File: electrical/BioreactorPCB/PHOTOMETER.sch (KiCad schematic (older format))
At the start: 9 parts, among them IC2 VEML7700-TR, J11 Conn_01x06_Male, U4 TCA39306DCUR

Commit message: Converted all nonpolarized resistors and capacitors to SMD. USB now has differential pairs that conform to design guidelines. Lots of traces, to what end? idk.
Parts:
- R8: footprint Resistor_THT:R_Axial_DIN0207_L6.3mm_D2.5mm_P10.16mm_Horizontal -> Resistor_SMD:R_0805_2012Metric_Pad1.20x1.40mm_HandSolder
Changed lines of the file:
@@
 F 0 "R8" V 7693 2425 50  0000 C CNN
 F 1 "200K" V 7784 2425 50  0000 C CNN
-F 2 "Resistor_THT:R_Axial_DIN0207_L6.3mm_D2.5mm_P10.16mm_Horizontal" V 7830 2425 50  0001 C CNN
+F 2 "Resistor_SMD:R_0805_2012Metric_Pad1.20x1.40mm_HandSolder" V 7830 2425 50  0001 C CNN
 F 3 "~" H 7900 2425 50  0001 C CNN
 	1    7900 2425

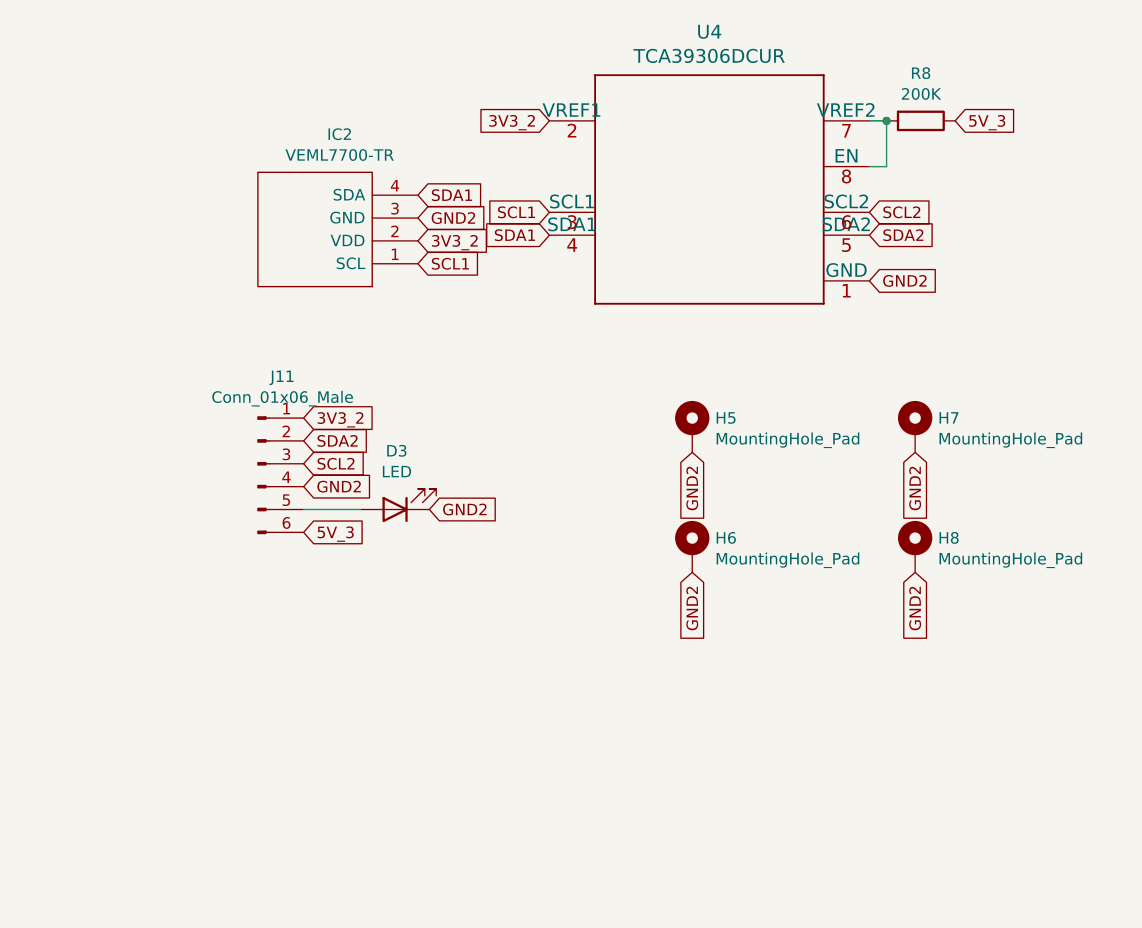
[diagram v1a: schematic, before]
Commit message: changed layout and schematic to reflect addition of a third daughterboard and separation of the LED and photodiode onto separate boards
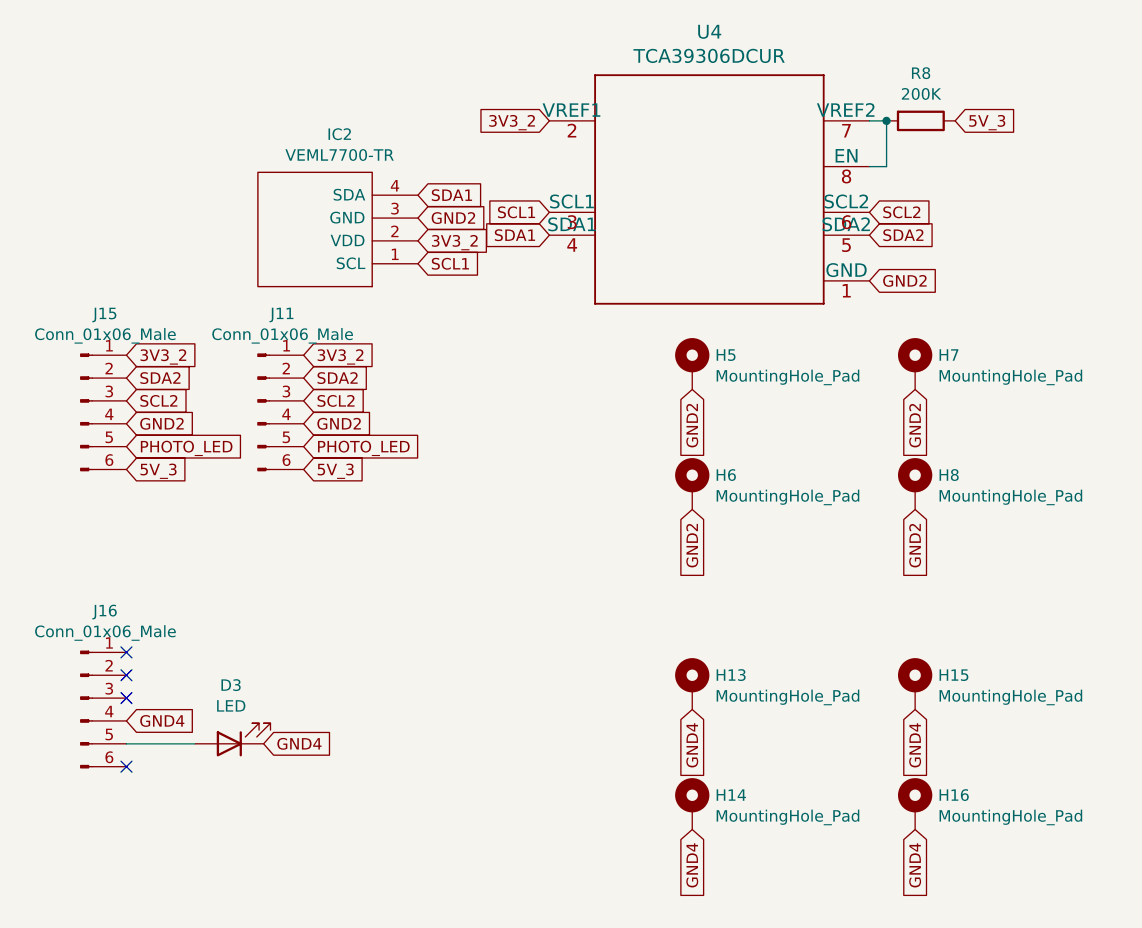
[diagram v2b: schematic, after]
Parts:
- added H13, H14, H15, H16: MountingHole_Pad, MountingHole:MountingHole_3.2mm_M3_DIN965_Pad, symbol Mechanical:MountingHole_Pad
- added J15, J16: Conn_01x06_Male, Connector_Molex:Molex_KK-254_AE-6410-06A_1x06_P2.54mm_Vertical, symbol Connector:Conn_01x06_Male
- D3: footprint LED_THT:LED_D5.0mm_Horizontal_O3.81mm_Z9.0mm -> LED_THT:LED_D5.0mm
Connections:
- net 3V3_2: now also J15.1 (Pin_1)
- net 5V_3: now also J15.6 (Pin_6)
- net GND2: now also J15.4 (Pin_4); no longer D3.1 (K)
- net SCL2: now also J15.3 (Pin_3)
- net SDA2: now also J15.2 (Pin_2)
- net at D3.2 (A): now also J16.5 (Pin_5); no longer J11.5 (Pin_5)
- new net GND4: D3.1 (K), H13.1, H14.1, H15.1, H16.1, J16.4 (Pin_4)
- new net PHOTO_LED: J11.5 (Pin_5), J15.5 (Pin_5)
- no-connect marks 0 -> 4
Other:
- moved on the sheet: D3, H5, H6, H7, H8, J11
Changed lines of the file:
@@
 L Device:LED D?
 U 1 1 62075D59
-P 5600 4125
+P 4875 5150
 AR Path="/62075D59" Ref="D?"  Part="1"
 AR Path="/62072BBC/62075D59" Ref="D3"  Part="1"
-F 0 "D3" H 5593 3870 50  0000 C CNN
-F 1 "LED" H 5593 3961 50  0000 C CNN
-F 2 "LED_THT:LED_D5.0mm_Horizontal_O3.81mm_Z9.0mm" H 5600 4125 50  0001 C CNN
-F 3 "~" H 5600 4125 50  0001 C CNN
-	1    5600 4125
+F 0 "D3" H 4868 4895 50  0000 C CNN
+F 1 "LED" H 4868 4986 50  0000 C CNN
+F 2 "LED_THT:LED_D5.0mm" H 4875 5150 50  0001 C CNN
+F 3 "~" H 4875 5150 50  0001 C CNN
+	1    4875 5150
 	-1   0    0    1
 $EndComp
-Text GLabel 5750 4125 2    50   Input ~ 0
-GND2
+Text GLabel 5025 5150 2    50   Input ~ 0
+GND4
 $Comp
 L Connector:Conn_01x06_Male J?
 U 1 1 62075D66
-P 5000 3925
+P 5000 3650
 AR Path="/62075D66" Ref="J?"  Part="1"
 AR Path="/62072BBC/62075D66" Ref="J11"  Part="1"
-F 0 "J11" H 5108 4306 50  0000 C CNN
-F 1 "Conn_01x06_Male" H 5108 4215 50  0000 C CNN
-F 2 "Connector_Molex:Molex_KK-254_AE-6410-06A_1x06_P2.54mm_Vertical" H 5000 3925 50  0001 C CNN
-F 3 "~" H 5000 3925 50  0001 C CNN
-	1    5000 3925
+F 0 "J11" H 5108 4031 50  0000 C CNN
+F 1 "Conn_01x06_Male" H 5108 3940 50  0000 C CNN
+F 2 "Connector_Molex:Molex_KK-254_AE-6410-06A_1x06_P2.54mm_Vertical" H 5000 3650 50  0001 C CNN
+F 3 "~" H 5000 3650 50  0001 C CNN
+	1    5000 3650
 	1    0    0    -1
 $EndComp
 Text GLabel 7675 3125 2    50   Input ~ 0
 GND2
-Text GLabel 5200 4225 2    50   Input ~ 0
+Text GLabel 5200 3950 2    50   Input ~ 0
 5V_3
 Text GLabel 8050 2425 2    50   Input ~ 0
@@
 	0    1    1    0
 $EndComp
-Text GLabel 5200 3725 2    50   Input ~ 0
+Text GLabel 5200 3450 2    50   Input ~ 0
 3V3_2
 Text GLabel 6275 2425 0    50   Input ~ 0
@@
 Text GLabel 5700 2850 2    50   Input ~ 0
 GND2
-Text GLabel 5200 3925 2    50   Input ~ 0
+Text GLabel 5200 3650 2    50   Input ~ 0
 SCL2
-Text GLabel 5200 4025 2    50   Input ~ 0
-GND2
-Wire Wire Line
-	5200 4125 5450 4125
-Text GLabel 5200 3825 2    50   Input ~ 0
+Text GLabel 5200 3750 2    50   Input ~ 0
+GND2
+Text GLabel 5200 3550 2    50   Input ~ 0
 SDA2
 Text GLabel 7675 2825 2    50   Input ~ 0
@@
 L Mechanical:MountingHole_Pad H?
 U 1 1 6207BB37
-P 6900 3775
+P 6900 3500
 AR Path="/6207BB37" Ref="H?"  Part="1"
 AR Path="/62072BBC/6207BB37" Ref="H5"  Part="1"
-F 0 "H5" H 7000 3824 50  0000 L CNN
-F 1 "MountingHole_Pad" H 7000 3733 50  0000 L CNN
-F 2 "MountingHole:MountingHole_3.2mm_M3_DIN965_Pad" H 6900 3775 50  0001 C CNN
-F 3 "~" H 6900 3775 50  0001 C CNN
-	1    6900 3775
+F 0 "H5" H 7000 3549 50  0000 L CNN
+F 1 "MountingHole_Pad" H 7000 3458 50  0000 L CNN
+F 2 "MountingHole:MountingHole_3.2mm_M3_DIN965_Pad" H 6900 3500 50  0001 C CNN
+F 3 "~" H 6900 3500 50  0001 C CNN
+	1    6900 3500
 	1    0    0    -1
 $EndComp
@@
 L Mechanical:MountingHole_Pad H?
 U 1 1 6207BB43
-P 7875 4300
+P 7875 4025
 AR Path="/6207BB43" Ref="H?"  Part="1"
 AR Path="/62072BBC/6207BB43" Ref="H8"  Part="1"
-F 0 "H8" H 7975 4349 50  0000 L CNN
-F 1 "MountingHole_Pad" H 7975 4258 50  0000 L CNN
-F 2 "MountingHole:MountingHole_3.2mm_M3_DIN965_Pad" H 7875 4300 50  0001 C CNN
-F 3 "~" H 7875 4300 50  0001 C CNN
-	1    7875 4300
+F 0 "H8" H 7975 4074 50  0000 L CNN
+F 1 "MountingHole_Pad" H 7975 3983 50  0000 L CNN
+F 2 "MountingHole:MountingHole_3.2mm_M3_DIN965_Pad" H 7875 4025 50  0001 C CNN
+F 3 "~" H 7875 4025 50  0001 C CNN
+	1    7875 4025
 	1    0    0    -1
 $EndComp
@@
 L Mechanical:MountingHole_Pad H?
 U 1 1 6207BB49
-P 7875 3775
+P 7875 3500
 AR Path="/6207BB49" Ref="H?"  Part="1"
 AR Path="/62072BBC/6207BB49" Ref="H7"  Part="1"
-F 0 "H7" H 7975 3824 50  0000 L CNN
-F 1 "MountingHole_Pad" H 7975 3733 50  0000 L CNN
-F 2 "MountingHole:MountingHole_3.2mm_M3_DIN965_Pad" H 7875 3775 50  0001 C CNN
-F 3 "~" H 7875 3775 50  0001 C CNN
-	1    7875 3775
-	1    0    0    -1
-$EndComp
-Text GLabel 6900 4400 3    50   Input ~ 0
-GND2
-Text GLabel 7875 3875 3    50   Input ~ 0
-GND2
-Text GLabel 7875 4400 3    50   Input ~ 0
+F 0 "H7" H 7975 3549 50  0000 L CNN
+F 1 "MountingHole_Pad" H 7975 3458 50  0000 L CNN
+F 2 "MountingHole:MountingHole_3.2mm_M3_DIN965_Pad" H 7875 3500 50  0001 C CNN
+F 3 "~" H 7875 3500 50  0001 C CNN
+	1    7875 3500
+	1    0    0    -1
+$EndComp
+Text GLabel 6900 4125 3    50   Input ~ 0
+GND2
+Text GLabel 7875 3600 3    50   Input ~ 0
+GND2
+Text GLabel 7875 4125 3    50   Input ~ 0
 GND2
 $Comp
@@
 L Mechanical:MountingHole_Pad H?
 U 1 1 6207BB3D
-P 6900 4300
+P 6900 4025
 AR Path="/6207BB3D" Ref="H?"  Part="1"
 AR Path="/62072BBC/6207BB3D" Ref="H6"  Part="1"
-F 0 "H6" H 7000 4349 50  0000 L CNN
-F 1 "MountingHole_Pad" H 7000 4258 50  0000 L CNN
-F 2 "MountingHole:MountingHole_3.2mm_M3_DIN965_Pad" H 6900 4300 50  0001 C CNN
-F 3 "~" H 6900 4300 50  0001 C CNN
-	1    6900 4300
-	1    0    0    -1
-$EndComp
-Text GLabel 6900 3875 3    50   Input ~ 0
-GND2
+F 0 "H6" H 7000 4074 50  0000 L CNN
+F 1 "MountingHole_Pad" H 7000 3983 50  0000 L CNN
+F 2 "MountingHole:MountingHole_3.2mm_M3_DIN965_Pad" H 6900 4025 50  0001 C CNN
+F 3 "~" H 6900 4025 50  0001 C CNN
+	1    6900 4025
+	1    0    0    -1
+$EndComp
+Text GLabel 6900 3600 3    50   Input ~ 0
+GND2
+$Comp
+L Connector:Conn_01x06_Male J?
+U 1 1 61D951CB
+P 4225 4950
+AR Path="/61D951CB" Ref="J?"  Part="1"
+AR Path="/62072BBC/61D951CB" Ref="J16"  Part="1"
+F 0 "J16" H 4333 5331 50  0000 C CNN
+F 1 "Conn_01x06_Male" H 4333 5240 50  0000 C CNN
+F 2 "Connector_Molex:Molex_KK-254_AE-6410-06A_1x06_P2.54mm_Vertical" H 4225 4950 50  0001 C CNN
+F 3 "~" H 4225 4950 50  0001 C CNN
+	1    4225 4950
+	1    0    0    -1
+$EndComp
+Text GLabel 4425 5050 2    50   Input ~ 0
+GND4
+$Comp
+L Connector:Conn_01x06_Male J?
+U 1 1 61D98646
+P 4225 3650
+AR Path="/61D98646" Ref="J?"  Part="1"
+AR Path="/62072BBC/61D98646" Ref="J15"  Part="1"
+F 0 "J15" H 4333 4031 50  0000 C CNN
+F 1 "Conn_01x06_Male" H 4333 3940 50  0000 C CNN
+F 2 "Connector_Molex:Molex_KK-254_AE-6410-06A_1x06_P2.54mm_Vertical" H 4225 3650 50  0001 C CNN
+F 3 "~" H 4225 3650 50  0001 C CNN
+	1    4225 3650
+	1    0    0    -1
+$EndComp
+Text GLabel 4425 3950 2    50   Input ~ 0
+5V_3
+Text GLabel 4425 3450 2    50   Input ~ 0
+3V3_2
+Text GLabel 4425 3650 2    50   Input ~ 0
+SCL2
+Text GLabel 4425 3750 2    50   Input ~ 0
+GND2
+Text GLabel 4425 3550 2    50   Input ~ 0
+SDA2
+Wire Wire Line
+	4425 5150 4725 5150
+NoConn ~ 4425 4750
+NoConn ~ 4425 4850
+NoConn ~ 4425 4950
+NoConn ~ 4425 5250
+$Comp
+L Mechanical:MountingHole_Pad H?
+U 1 1 61DB2012
+P 6900 4900
+AR Path="/61DB2012" Ref="H?"  Part="1"
+AR Path="/62072BBC/61DB2012" Ref="H13"  Part="1"
+F 0 "H13" H 7000 4949 50  0000 L CNN
+F 1 "MountingHole_Pad" H 7000 4858 50  0000 L CNN
+F 2 "MountingHole:MountingHole_3.2mm_M3_DIN965_Pad" H 6900 4900 50  0001 C CNN
+F 3 "~" H 6900 4900 50  0001 C CNN
+	1    6900 4900
+	1    0    0    -1
+$EndComp
+$Comp
+L Mechanical:MountingHole_Pad H?
+U 1 1 61DB2018
+P 7875 5425
+AR Path="/61DB2018" Ref="H?"  Part="1"
+AR Path="/62072BBC/61DB2018" Ref="H16"  Part="1"
+F 0 "H16" H 7975 5474 50  0000 L CNN
+F 1 "MountingHole_Pad" H 7975 5383 50  0000 L CNN
+F 2 "MountingHole:MountingHole_3.2mm_M3_DIN965_Pad" H 7875 5425 50  0001 C CNN
+F 3 "~" H 7875 5425 50  0001 C CNN
+	1    7875 5425
+	1    0    0    -1
+$EndComp
+$Comp
+L Mechanical:MountingHole_Pad H?
+U 1 1 61DB201E
+P 7875 4900
+AR Path="/61DB201E" Ref="H?"  Part="1"
+AR Path="/62072BBC/61DB201E" Ref="H15"  Part="1"
+F 0 "H15" H 7975 4949 50  0000 L CNN
+F 1 "MountingHole_Pad" H 7975 4858 50  0000 L CNN
+F 2 "MountingHole:MountingHole_3.2mm_M3_DIN965_Pad" H 7875 4900 50  0001 C CNN
+F 3 "~" H 7875 4900 50  0001 C CNN
+	1    7875 4900
+	1    0    0    -1
+$EndComp
+Text GLabel 6900 5525 3    50   Input ~ 0
+GND4
+Text GLabel 7875 5000 3    50   Input ~ 0
+GND4
+Text GLabel 7875 5525 3    50   Input ~ 0
+GND4
+$Comp
+L Mechanical:MountingHole_Pad H?
+U 1 1 61DB2027
+P 6900 5425
+AR Path="/61DB2027" Ref="H?"  Part="1"
+AR Path="/62072BBC/61DB2027" Ref="H14"  Part="1"
+F 0 "H14" H 7000 5474 50  0000 L CNN
+F 1 "MountingHole_Pad" H 7000 5383 50  0000 L CNN
+F 2 "MountingHole:MountingHole_3.2mm_M3_DIN965_Pad" H 6900 5425 50  0001 C CNN
+F 3 "~" H 6900 5425 50  0001 C CNN
+	1    6900 5425
+	1    0    0    -1
+$EndComp
+Text GLabel 6900 5000 3    50   Input ~ 0
+GND4
+Text GLabel 5200 3850 2    50   Input ~ 0
+PHOTO_LED
+Text GLabel 4425 3850 2    50   Input ~ 0
+PHOTO_LED
 $EndSCHEMATC
